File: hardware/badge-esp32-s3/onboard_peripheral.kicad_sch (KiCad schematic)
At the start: 0 parts

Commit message: Reapply "Merge branch 'main' into Danny"
This reverts commit 522ccfdb580e54901b8ff562dc2e90cfc327c6b7.
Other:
- added sheet Accelormeter (Accelormeter.kicad_sch)
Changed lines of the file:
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@@
+	)
+	(sheet
+		(at 53.34 153.67)
+		(size 24.13 11.43)
+		(exclude_from_sim no)
+		(in_bom yes)
+		(on_board yes)
+		(dnp no)
+		(fields_autoplaced yes)
+		(stroke
+			(width 0.1524)
+			(type solid)
+		)
+		(fill
+			(color 0 0 0 0.0000)
+		)
+		(property "Sheetname" "Accelormeter"
+			(at 53.34 152.9584 0)
+			(effects
+				(font
+					(size 1.27 1.27)
+				)
+				(justify left bottom)
+			)
+		)
+		(property "Sheetfile" "Accelormeter.kicad_sch"
+			(at 53.34 165.6846 0)
+			(effects
+				(font
+					(size 1.27 1.27)
+				)
+				(justify left top)
+			)
+		)
+		(instances
+			(project "badge-esp32-s3"
+				(path "/e2af9a6c-dbe9-4de2-9ba6-ea213a7300ec/9feb22ac-0492-47b5-89fe-3e77a54de168"
+					(page "22")
+				)
+			)
+		)
 	)
 	(sheet

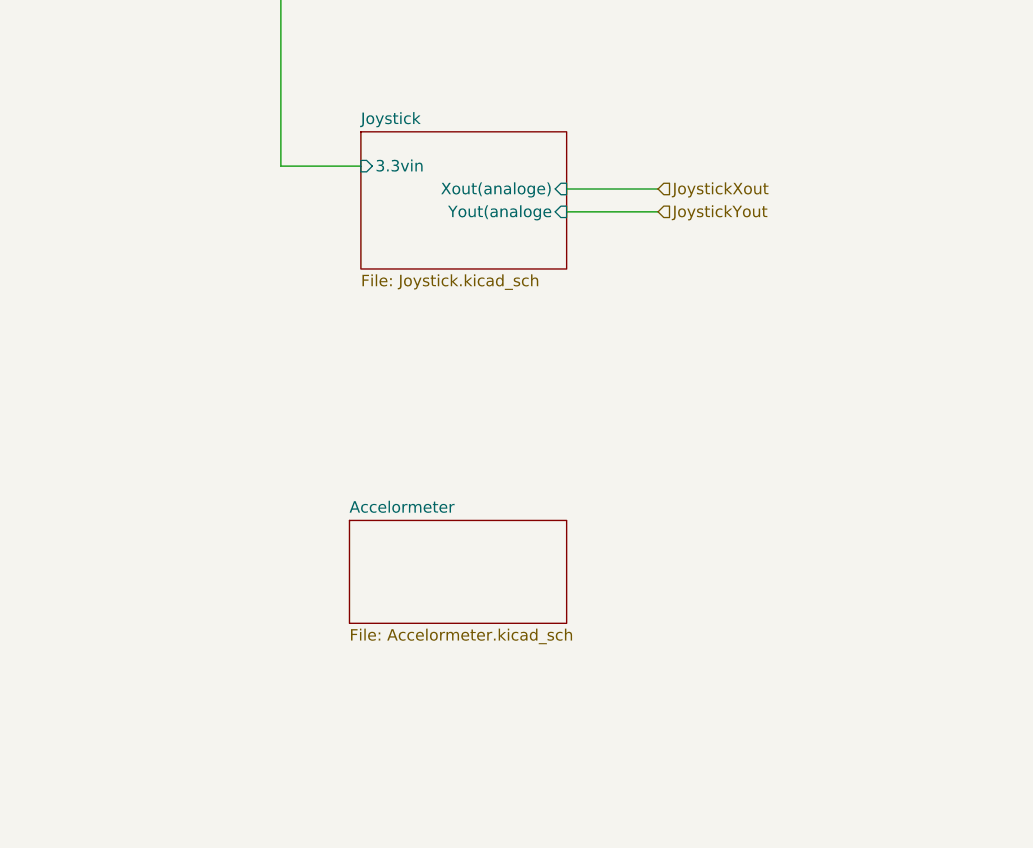
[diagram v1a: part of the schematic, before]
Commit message: Fleshed out schematic with all exposed pins
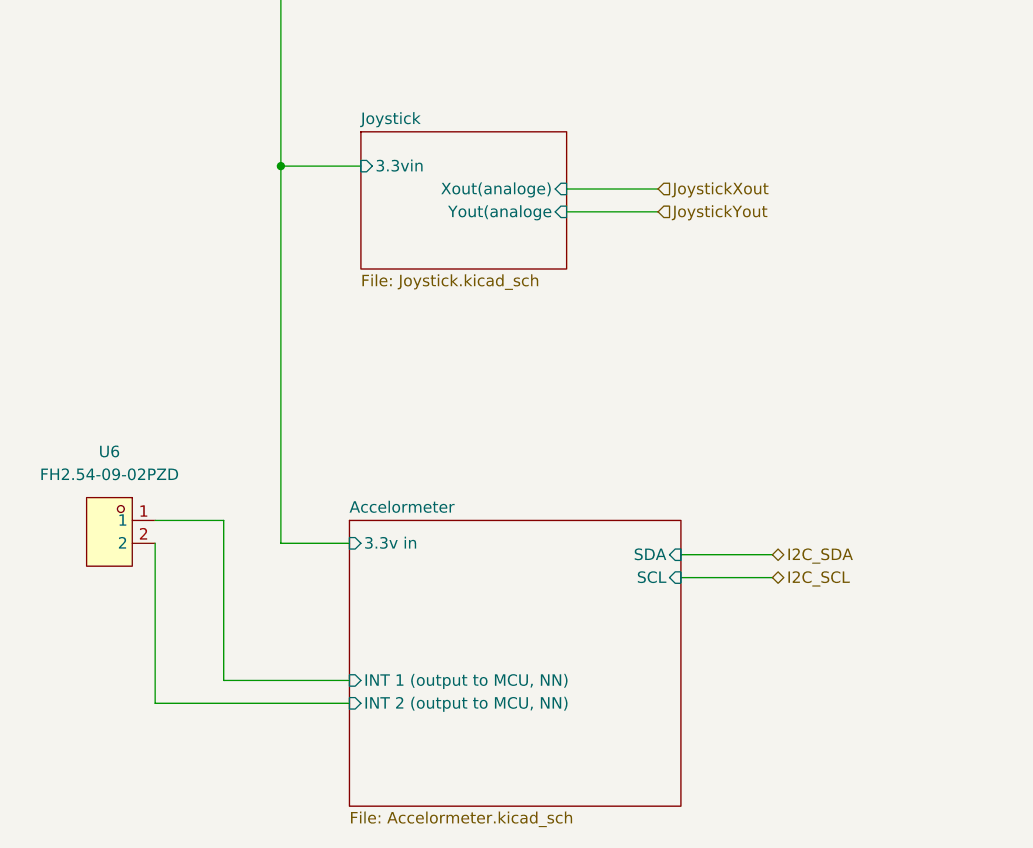
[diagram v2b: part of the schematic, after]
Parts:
- added U6: FH2.54-09-02PZD, lcsc-lib:HDR-TH_2P-P2.54-V-M-5, symbol lcsc-lib:FH2.54-09-02PZD
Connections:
- new net Accelormeter/INT 1 (output to MCU, NN) : U6.1
- new net Accelormeter/INT 2 (output to MCU, NN) : U6.2
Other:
- sheet Accelormeter ports: added 3.3v in, INT 1 (output to MCU, NN) , INT 2 (output to MCU, NN) , SCL, SDA; removed none
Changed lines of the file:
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@@
 	(paper "A4")
+	(junction
+		(at 45.72 114.3)
+		(diameter 0)
+		(color 0 0 0 0)
+	)
 	(junction
 		(at 158.75 41.91)
@@
 	(wire
 		(pts
+			(xy 39.37 153.67) (xy 39.37 171.45)
+		)
+		(stroke
+			(width 0)
+			(type default)
+		)
+	)
+	(wire
+		(pts
 			(xy 107.95 41.91) (xy 107.95 71.12)
 		)
@@
 	(wire
 		(pts
+			(xy 39.37 153.67) (xy 31.75 153.67)
+		)
+		(stroke
+			(width 0)
+			(type default)
+		)
+	)
+	(wire
+		(pts
 			(xy 78.74 78.74) (xy 74.93 78.74)
 		)
@@
 	(wire
 		(pts
+			(xy 53.34 173.99) (xy 31.75 173.99)
+		)
+		(stroke
+			(width 0)
+			(type default)
+		)
+	)
+	(wire
+		(pts
 			(xy 158.75 63.5) (xy 158.75 41.91)
 		)
@@
 	(wire
 		(pts
+			(xy 90.17 160.02) (xy 100.33 160.02)
+		)
+		(stroke
+			(width 0)
+			(type default)
+		)
+	)
+	(wire
+		(pts
 			(xy 45.72 114.3) (xy 45.72 41.91)
 		)
@@
 	(wire
 		(pts
+			(xy 53.34 156.21) (xy 45.72 156.21)
+		)
+		(stroke
+			(width 0)
+			(type default)
+		)
+	)
+	(wire
+		(pts
+			(xy 45.72 156.21) (xy 45.72 114.3)
+		)
+		(stroke
+			(width 0)
+			(type default)
+		)
+	)
+	(wire
+		(pts
+			(xy 31.75 156.21) (xy 31.75 173.99)
+		)
+		(stroke
+			(width 0)
+			(type default)
+		)
+	)
+	(wire
+		(pts
 			(xy 149.86 60.96) (xy 149.86 71.12)
 		)
@@
 		(pts
 			(xy 146.05 80.01) (xy 146.05 78.74)
+		)
+		(stroke
+			(width 0)
+			(type default)
+		)
+	)
+	(wire
+		(pts
+			(xy 53.34 171.45) (xy 39.37 171.45)
+		)
+		(stroke
+			(width 0)
+			(type default)
+		)
+	)
+	(wire
+		(pts
+			(xy 90.17 157.48) (xy 100.33 157.48)
 		)
 		(stroke
@@
 		)
 	)
+	(hierarchical_label "I2C_SCL"
+		(shape bidirectional)
+		(at 100.33 160.02 0)
+		(effects
+			(font
+				(size 1.27 1.27)
+			)
+			(justify left)
+		)
+	)
 	(hierarchical_label "RightbuttonGPIO"
 		(shape input)
@@
 		)
 	)
+	(hierarchical_label "I2C_SDA"
+		(shape bidirectional)
+		(at 100.33 157.48 0)
+		(effects
+			(font
+				(size 1.27 1.27)
+			)
+			(justify left)
+		)
+	)
 	(hierarchical_label "JoystickXout"
 		(shape input)
@@
 			)
 			(justify left)
+		)
+	)
+	(symbol
+		(lib_id "lcsc-lib:FH2.54-09-02PZD")
+		(at 26.67 154.94 0)
+		(mirror y)
+		(unit 1)
+		(exclude_from_sim no)
+		(in_bom yes)
+		(on_board yes)
+		(dnp no)
+		(fields_autoplaced yes)
+		(property "Reference" "U6"
+			(at 26.67 146.05 0)
+			(effects
+				(font
+					(size 1.27 1.27)
+				)
+			)
+		)
+		(property "Value" "FH2.54-09-02PZD"
+			(at 26.67 148.59 0)
+			(effects
+				(font
+					(size 1.27 1.27)
+				)
+			)
+		)
+		(property "Footprint" "lcsc-lib:HDR-TH_2P-P2.54-V-M-5"
+			(at 26.67 163.83 0)
+			(effects
+				(font
+					(size 1.27 1.27)
+				)
+				(hide yes)
+			)
+		)
+		(property "Datasheet" ""
+			(at 26.67 154.94 0)
+			(effects
+				(font
+					(size 1.27 1.27)
+				)
+				(hide yes)
+			)
+		)
+		(property "Description" ""
+			(at 26.67 154.94 0)
+			(effects
+				(font
+					(size 1.27 1.27)
+				)
+				(hide yes)
+			)
+		)
+		(property "LCSC Part" "C7500771"
+			(at 26.67 166.37 0)
+			(effects
+				(font
+					(size 1.27 1.27)
+				)
+				(hide yes)
+			)
+		)
+		(pin "2"
+		)
+		(pin "1"
+		)
+		(instances
+			(project ""
+				(path "/e2af9a6c-dbe9-4de2-9ba6-ea213a7300ec/9feb22ac-0492-47b5-89fe-3e77a54de168"
+					(reference "U6")
+					(unit 1)
+				)
+			)
 		)
 	)
@@
 	(sheet
 		(at 53.34 153.67)
-		(size 24.13 11.43)
+		(size 36.83 31.75)
 		(exclude_from_sim no)
 		(in_bom yes)
@@
 		)
 		(property "Sheetfile" "Accelormeter.kicad_sch"
-			(at 53.34 165.6846 0)
+			(at 53.34 186.0046 0)
 			(effects
 				(font
@@
 			)
 		)
+		(pin "INT 1 (output to MCU, NN) " input
+			(at 53.34 171.45 180)
+			(effects
+				(font
+					(size 1.27 1.27)
+				)
+				(justify left)
+			)
+		)
+		(pin "SCL" input
+			(at 90.17 160.02 0)
+			(effects
+				(font
+					(size 1.27 1.27)
+				)
+				(justify right)
+			)
+		)
+		(pin "SDA" input
+			(at 90.17 157.48 0)
+			(effects
+				(font
+					(size 1.27 1.27)
+				)
+				(justify right)
+			)
+		)
+		(pin "INT 2 (output to MCU, NN) " input
+			(at 53.34 173.99 180)
+			(effects
+				(font
+					(size 1.27 1.27)
+				)
+				(justify left)
+			)
+		)
+		(pin "3.3v in" input
+			(at 53.34 156.21 180)
+			(effects
+				(font
+					(size 1.27 1.27)
+				)
+				(justify left)
+			)
+		)

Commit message: Annotate schematic
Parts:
- renumbered U6 to U17
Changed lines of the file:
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@@
 		(dnp no)
 		(fields_autoplaced yes)
-		(property "Reference" "U6"
+		(property "Reference" "U17"
 			(at 26.67 146.05 0)
 			(effects
@@
 			(project ""
 				(path "/e2af9a6c-dbe9-4de2-9ba6-ea213a7300ec/9feb22ac-0492-47b5-89fe-3e77a54de168"
-					(reference "U6")
+					(reference "U17")
 					(unit 1)
 				)

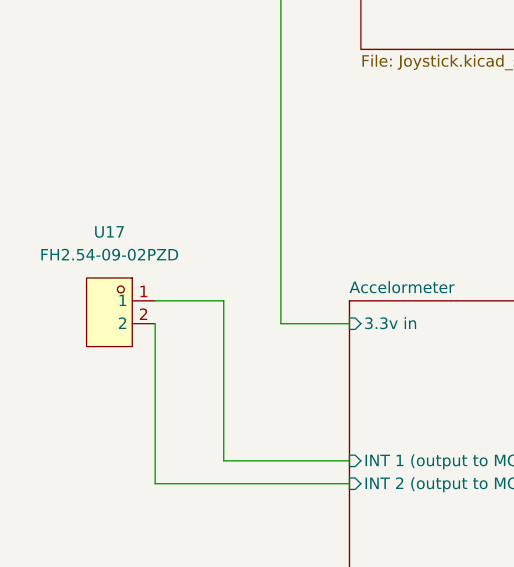
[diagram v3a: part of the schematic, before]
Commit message: Consolidated the GPIO pins, communication pins, and power pins.
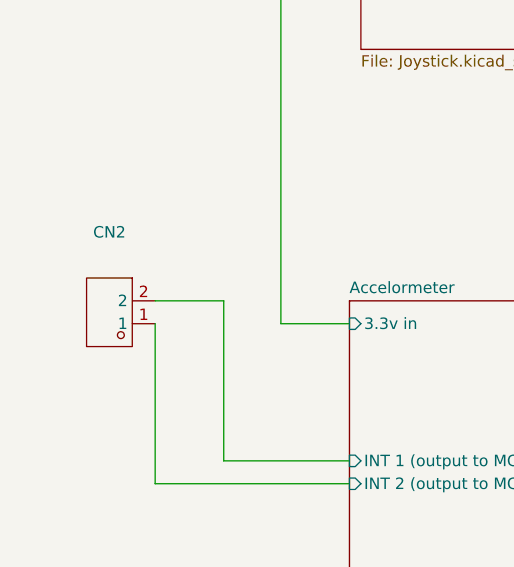
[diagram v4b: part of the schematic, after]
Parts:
- removed U17: FH2.54-09-02PZD, lcsc-lib:HDR-TH_2P-P2.54-V-M-5, symbol lcsc-lib:FH2.54-09-02PZD
- added CN2: ~, lcsc-lib:HDR-TH_2P-P2.54-V-F, symbol lcsc-lib:HX PM2.54-1X2P ZC-Y
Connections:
- net Accelormeter/INT 1 (output to MCU, NN) : now also CN2.2
- net Accelormeter/INT 2 (output to MCU, NN) : now also CN2.1
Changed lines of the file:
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@@
 	)
 	(symbol
-		(lib_id "lcsc-lib:FH2.54-09-02PZD")
-		(at 26.67 154.94 0)
-		(mirror y)
+		(lib_id "lcsc-lib:HX PM2.54-1X2P ZC-Y")
+		(at 26.67 154.94 180)
 		(unit 1)
 		(exclude_from_sim no)
@@
 		(dnp no)
 		(fields_autoplaced yes)
-		(property "Reference" "U17"
+		(property "Reference" "CN2"
 			(at 26.67 146.05 0)
 			(effects
@@
 			)
 		)
-		(property "Value" "FH2.54-09-02PZD"
+		(property "Value" "~"
 			(at 26.67 148.59 0)
 			(effects
@@
 			)
 		)
-		(property "Footprint" "lcsc-lib:HDR-TH_2P-P2.54-V-M-5"
-			(at 26.67 163.83 0)
-			(effects
-				(font
-					(size 1.27 1.27)
-				)
-				(hide yes)
-			)
-		)
-		(property "Datasheet" ""
+		(property "Footprint" "lcsc-lib:HDR-TH_2P-P2.54-V-F"
 			(at 26.67 154.94 0)
 			(effects
@@
 			)
 		)
-		(property "Description" ""
+		(property "Datasheet" "https://item.szlcsc.com/datasheet/HX%2520PM2.54-1x2P%2520ZC-Y/24075299.html"
 			(at 26.67 154.94 0)
 			(effects
@@
 			)
 		)
-		(property "LCSC Part" "C7500771"
-			(at 26.67 166.37 0)
+		(property "Description" "Holes Structure:1x2P Pitch:2.54mm Row Spacing:- Circular Hole / Square Hole:Square Hole Mounting Type:Through Hole Number of Rows:1 Number of Positions:2P Current Rating:3A Voltage Rating (Max):1kV Holes Direction:Top Insulation Height:8.5mm Contact Mater"
+			(at 26.67 154.94 0)
 			(effects
 				(font
@@
 			)
 		)
-		(pin "2"
+		(property "Manufacturer Part" "HX PM2.54-1x2P ZC-Y"
+			(at 26.67 154.94 0)
+			(effects
+				(font
+					(size 1.27 1.27)
+				)
+				(hide yes)
+			)
+		)
+		(property "Manufacturer" "hanxia(韩下)"
+			(at 26.67 154.94 0)
+			(effects
+				(font
+					(size 1.27 1.27)
+				)
+				(hide yes)
+			)
+		)
+		(property "Supplier Part" "C22438152"
+			(at 26.67 154.94 0)
+			(effects
+				(font
+					(size 1.27 1.27)
+				)
+				(hide yes)
+			)
+		)
+		(property "Supplier" "LCSC"
+			(at 26.67 154.94 0)
+			(effects
+				(font
+					(size 1.27 1.27)
+				)
+				(hide yes)
+			)
+		)
+		(property "LCSC Part Name" "1x2P 间距:2.54mm 直插"
+			(at 26.67 154.94 0)
+			(effects
+				(font
+					(size 1.27 1.27)
+				)
+				(hide yes)
+			)
 		)
 		(pin "1"
+		)
+		(pin "2"
 		)
 		(instances
 			(project ""
 				(path "/e2af9a6c-dbe9-4de2-9ba6-ea213a7300ec/9feb22ac-0492-47b5-89fe-3e77a54de168"
-					(reference "U17")
+					(reference "CN2")
 					(unit 1)
 				)

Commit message: minibadge_fix?
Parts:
- CN2: JLC_3DModel_Q (none) -> 925d5dffa823422895d76d9dc6f5e8cd; JLC_3D_Size (none) -> 5.48 2.5
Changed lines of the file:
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@@
+			)
+		)
+		(property "JLC_3DModel_Q" "925d5dffa823422895d76d9dc6f5e8cd"
+			(at 26.67 154.94 0)
+			(effects
+				(font
+					(size 1.27 1.27)
+				)
+				(hide yes)
+			)
+		)
+		(property "JLC_3D_Size" "5.48 2.5"
+			(at 26.67 154.94 0)
+			(effects
+				(font
+					(size 1.27 1.27)
+				)
+				(hide yes)
 			)
 		)

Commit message: Updated the wiring for the 5V line to be connected to the +4V net. That is what it is named even though it is 4.5 ish volts.
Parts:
- CN2: JLC_3DModel_Q 925d5dffa823422895d76d9dc6f5e8cd -> (none); JLC_3D_Size 5.48 2.5 -> (none)
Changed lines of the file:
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@@
-			)
-		)
-		(property "JLC_3DModel_Q" "925d5dffa823422895d76d9dc6f5e8cd"
-			(at 26.67 154.94 0)
-			(effects
-				(font
-					(size 1.27 1.27)
-				)
-				(hide yes)
-			)
-		)
-		(property "JLC_3D_Size" "5.48 2.5"
-			(at 26.67 154.94 0)
-			(effects
-				(font
-					(size 1.27 1.27)
-				)
-				(hide yes)
 			)
 		)

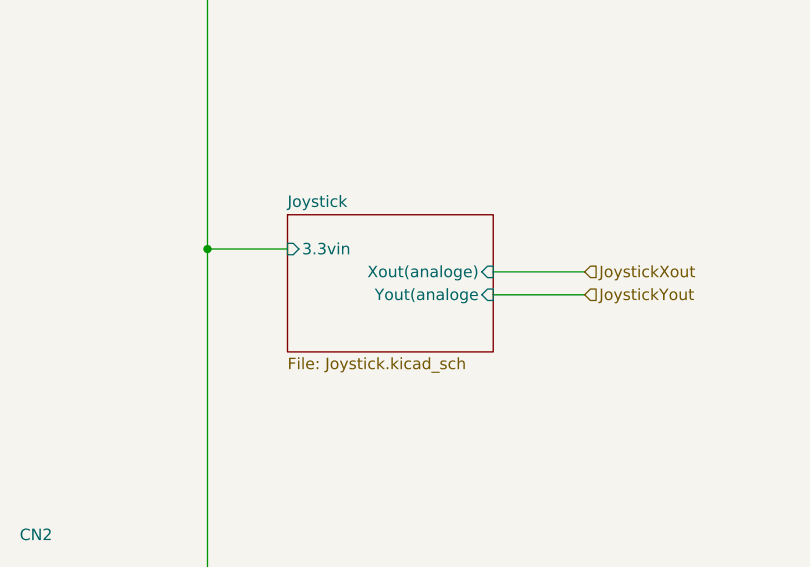
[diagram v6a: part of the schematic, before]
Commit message: added sdio
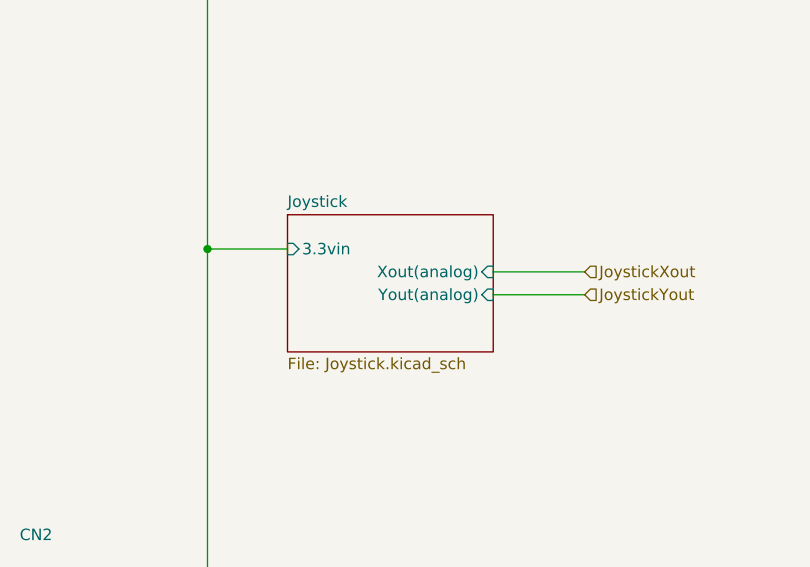
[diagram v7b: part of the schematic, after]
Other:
- sheet Joystick ports: added Xout(analog), Yout(analog); removed Xout(analoge), Yout(analoge
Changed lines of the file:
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@@
 			)
 		)
-		(pin "Xout(analoge)" input
+		(pin "Xout(analog)" input
 			(at 77.47 116.84 0)
 			(effects
@@
 			)
 		)
-		(pin "Yout(analoge" input
+		(pin "Yout(analog)" input
 			(at 77.47 119.38 0)
 			(effects
